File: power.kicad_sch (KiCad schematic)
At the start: 56 parts, among them J11 Conn_01x02_Pin, J13 Conn_01x02_Pin, J14 Conn_01x02_Pin, J15 Conn_01x02_Pin, J8 Conn_01x02_Pin, U10 MAX4995AAUT+T, U11 MAX4995AAUT+T, U35 MAX4995AAUT+T, U36 TPS7A5201QRGRRQ1, U4 TPSM828302ARDSR, U6 STWD100NYWY3F, U8 MP5073GG-P, U9 MAX4995AAUT+T

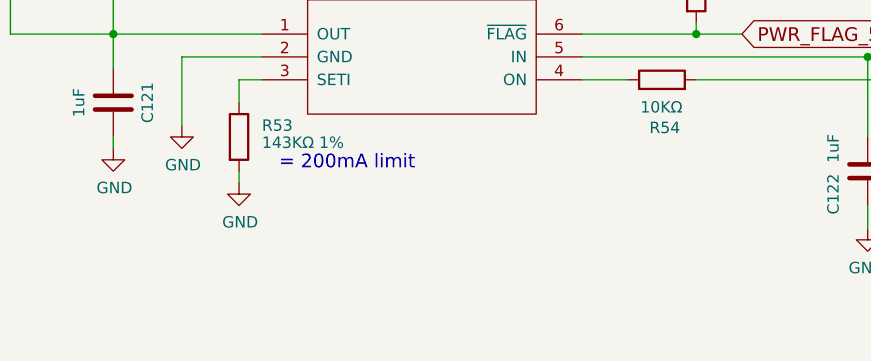
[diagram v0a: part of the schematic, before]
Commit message: Track and doc cleanups
Signed-off-by: Corey Minyard <corey@minyard.net>
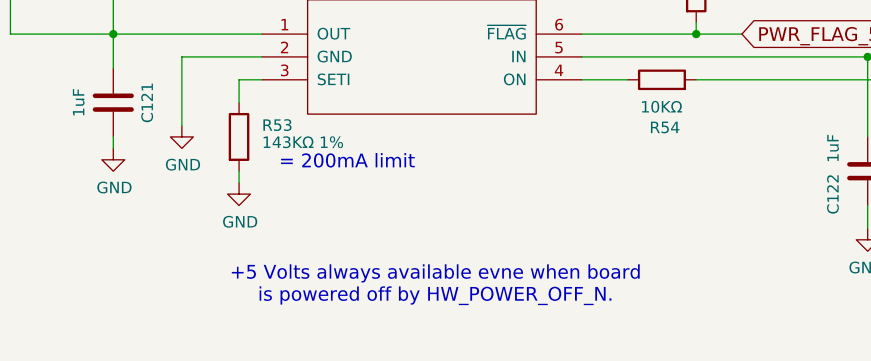
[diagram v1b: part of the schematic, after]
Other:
- note added: "+5 Volts always available evne when board is powered off by HW_POWER_OFF_N."
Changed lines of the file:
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@@
+		)
+	)
+	(text "+5 Volts always available evne when board\nis powered off by HW_POWER_OFF_N."
+		(exclude_from_sim no)
+		(at 233.934 257.81 0)
+		(effects
+			(font
+				(size 1.524 1.524)
+			)
 		)
 	)

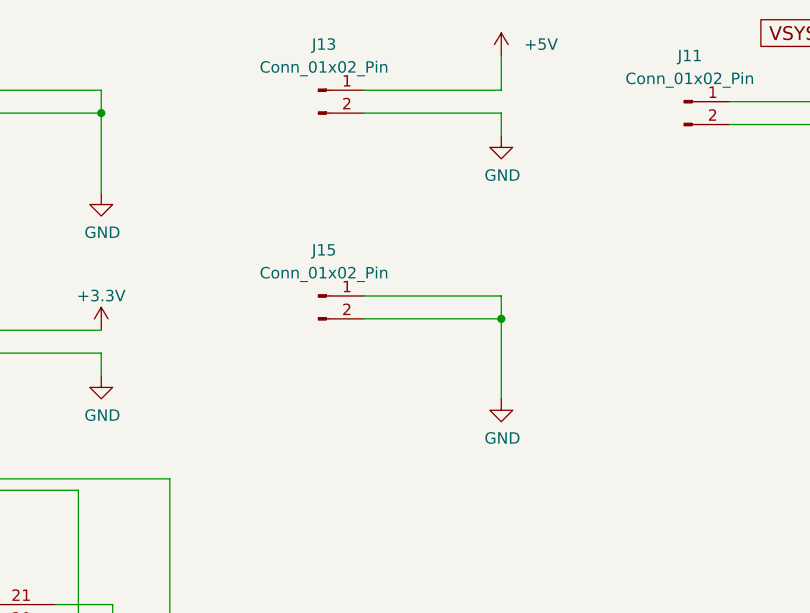
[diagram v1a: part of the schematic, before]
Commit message: Do a ton of work to switch to the CubeSat Kit Bus
Redo the connector, board shape, etc.

Signed-off-by: Corey Minyard <corey@minyard.net>
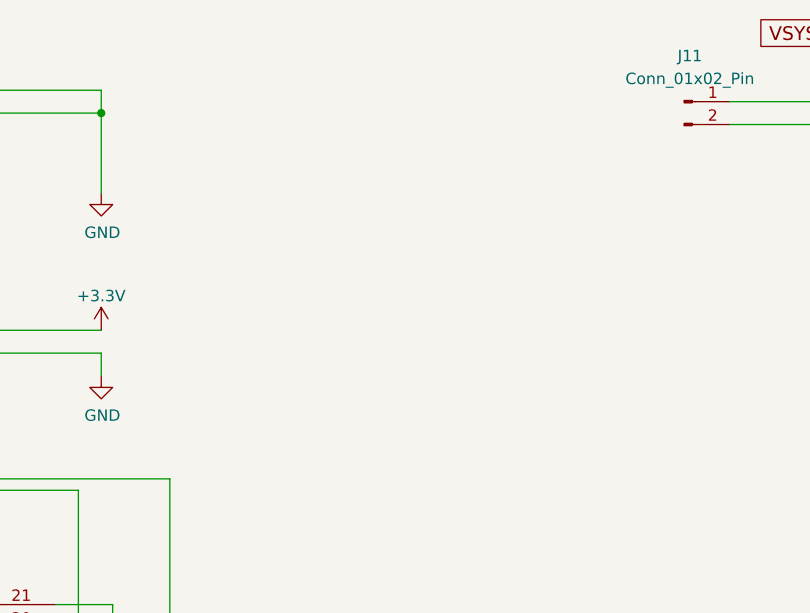
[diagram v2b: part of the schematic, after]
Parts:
- removed J13, J15: Conn_01x02_Pin, Connector_Wire:SolderWire-0.5sqmm_1x02_P4.6mm_D0.9mm_OD2.1mm, symbol Connector:Conn_01x02_Pin

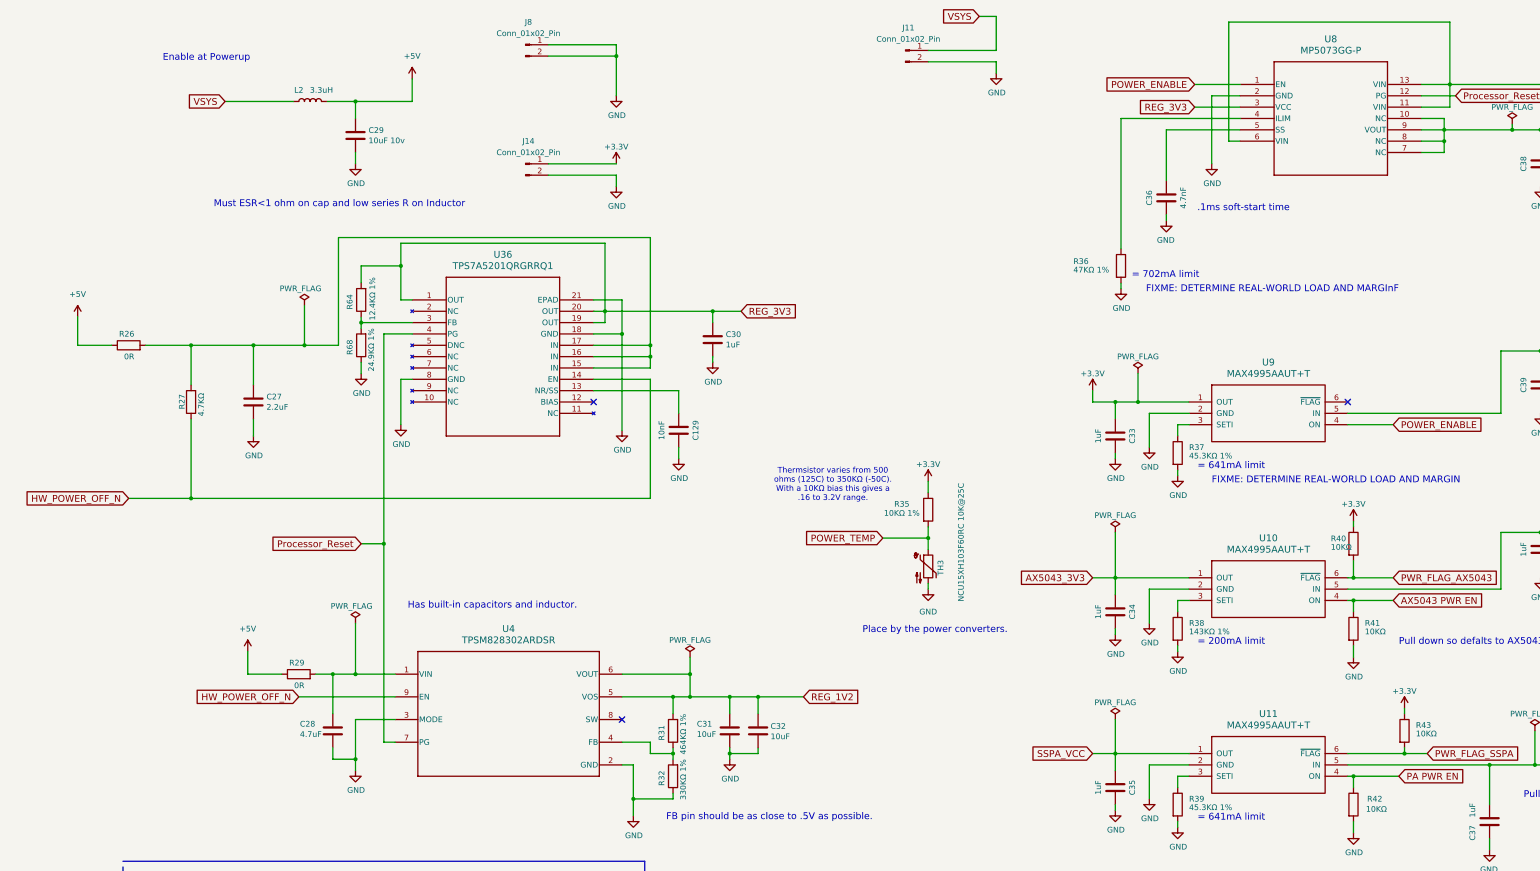
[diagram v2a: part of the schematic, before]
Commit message: More work converting to the CubeSat Kit Bus
Signed-off-by: Corey Minyard <corey@minyard.net>
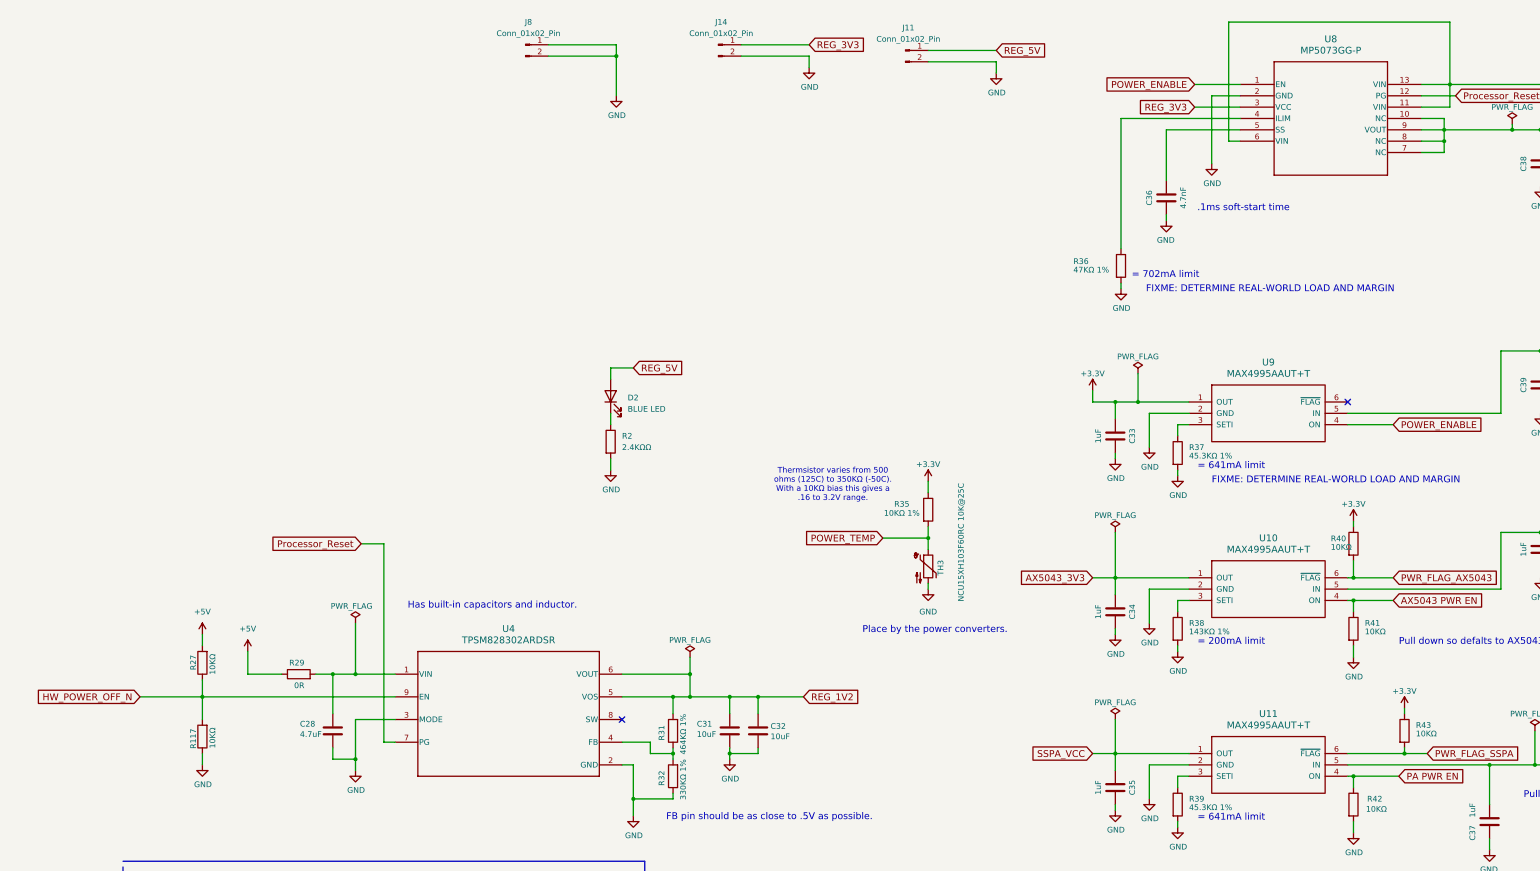
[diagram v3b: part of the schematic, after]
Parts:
- removed C129: 10nF, Capacitor_SMD:C_0402_1005Metric_Pad0.74x0.62mm_HandSolder, symbol Device:C
- removed C27: 2.2uF, Capacitor_SMD:C_0805_2012Metric_Pad1.18x1.45mm_HandSolder, symbol Device:C
- removed C29: 10uF 10v, Capacitor_SMD:C_1206_3216Metric, symbol Device:C
- removed C30: 1uF, Capacitor_SMD:C_0805_2012Metric_Pad1.18x1.45mm_HandSolder, symbol Device:C
- removed L2: 3.3uH, Inductor_SMD:L_1210_3225Metric_Pad1.42x2.65mm_HandSolder, symbol Device:L
- removed R26: 0R, Resistor_SMD:R_0603_1608Metric_Pad0.98x0.95mm_HandSolder, symbol Device:R
- removed R64: 12.4KΩ 1%, Resistor_SMD:R_0402_1005Metric_Pad0.72x0.64mm_HandSolder, symbol Device:R
- removed R68: 24.9KΩ 1%, Resistor_SMD:R_0402_1005Metric_Pad0.72x0.64mm_HandSolder, symbol Device:R
- removed U36: TPS7A5201QRGRRQ1, PacSatDev_ti:RGR20_2P05X2P05_TEX, symbol PACSAT_ICs:TPS7A5201QRGRRQ1
- added D2: BLUE LED, LED_SMD:LED_0603_1608Metric_Pad1.05x0.95mm_HandSolder, symbol Device:LED
- added R117: 10KΩ, Resistor_SMD:R_0402_1005Metric_Pad0.72x0.64mm_HandSolder, symbol Device:R
- added R2: 2.4KΩΩ, Resistor_SMD:R_0603_1608Metric_Pad0.98x0.95mm_HandSolder, symbol Device:R
- R27: value 4.7KΩ -> 10KΩ
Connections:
- net +3.3V: no longer J14.1 (Pin_1)
- net +5V: now also R27.2
- net GND: now also R117.1, R2.2
- net HW_POWER_OFF_N: now also R117.2
- net REG_3V3: now also J14.1 (Pin_1)
- net VSYS renamed REG_5V
- net REG_5V: now also D2.2 (A)
- new net: D2.1 (K), R2.1
- no-connect marks 3 -> 2
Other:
- note removed: "Enable at Powerup"
- note removed: "FIXME: DETERMINE REAL-WORLD LOAD AND MARGInF"
- note removed: "Must ESR<1 ohm on cap and low series R on Inductor"
- moved on the sheet: J14, R27

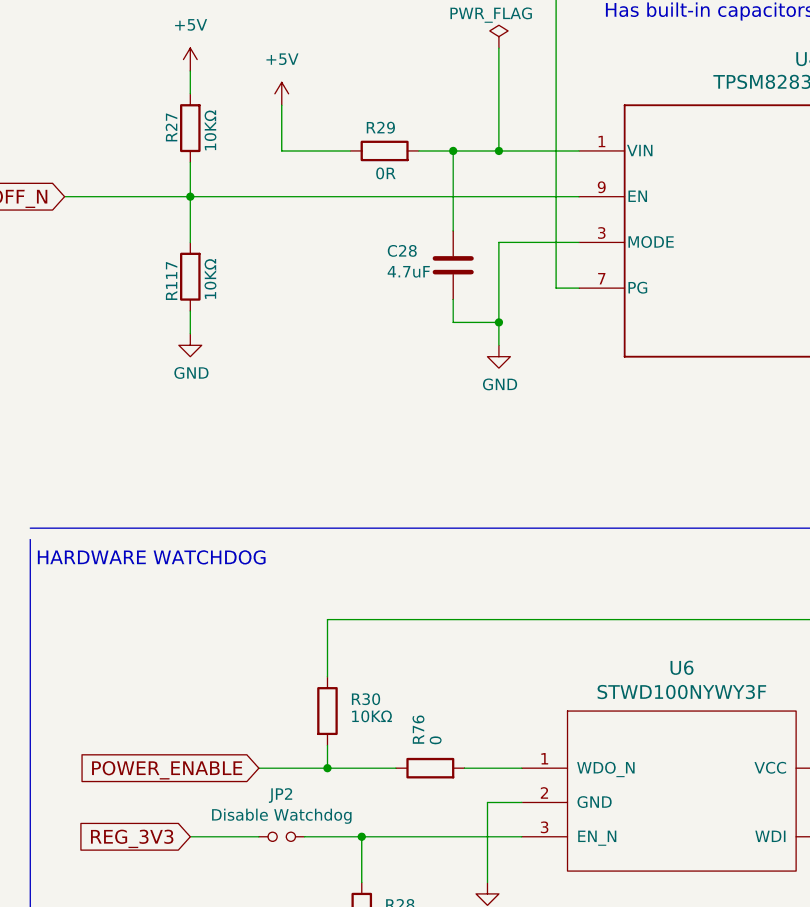
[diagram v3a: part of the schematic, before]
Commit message: Have the BOM file fixer output xls, not csv
The omega symbol gets translated properly from xls.

Signed-off-by: Corey Minyard <corey@minyard.net>
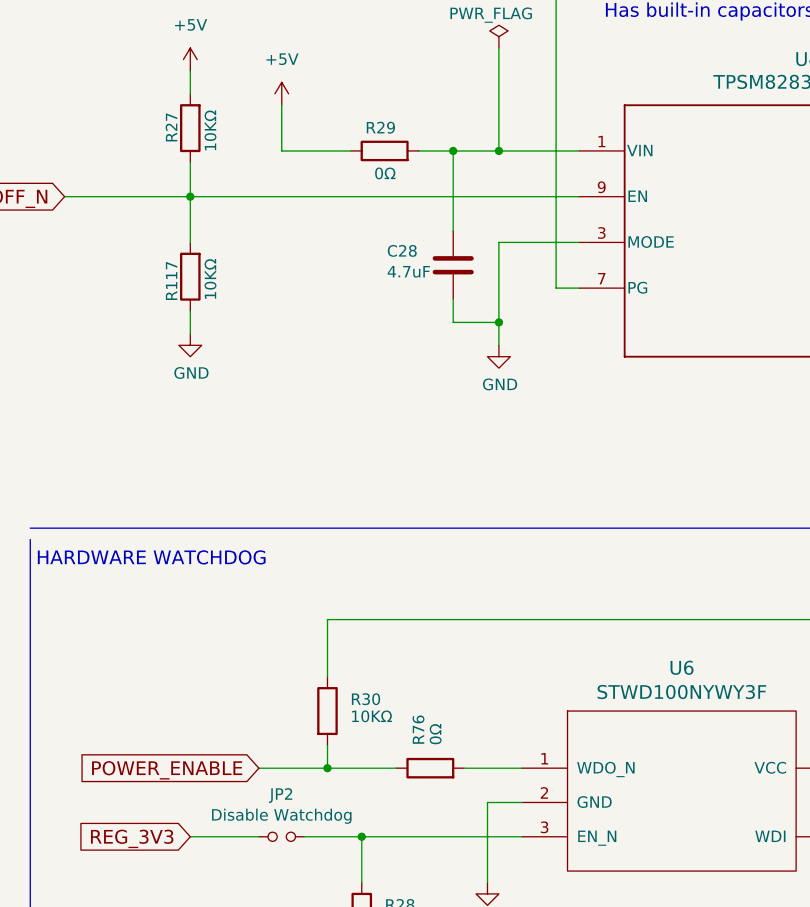
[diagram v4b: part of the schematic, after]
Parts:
- R29: value 0R -> 0Ω
- R76: value 0 -> 0Ω
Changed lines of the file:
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@@
 			)
 		)
-		(property "Value" "0R"
+		(property "Value" "0Ω"
 			(at 91.44 168.91 90)
 			(effects
@@
 			)
 		)
-		(property "Value" "0"
+		(property "Value" "0Ω"
 			(at 95.885 232.41 0)
 			(effects

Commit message: Minor fixes for BOM values
Signed-off-by: Corey Minyard <corey@minyard.net>
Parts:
- TH3: value NCU15XH103F60RC 10K@25C -> NCU15XH103F60RC 10KΩ@25C
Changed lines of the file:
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@@
 			)
 		)
-		(property "Value" "NCU15XH103F60RC 10K@25C"
+		(property "Value" "NCU15XH103F60RC 10KΩ@25C"
 			(at 238.506 150.114 90)
 			(effects

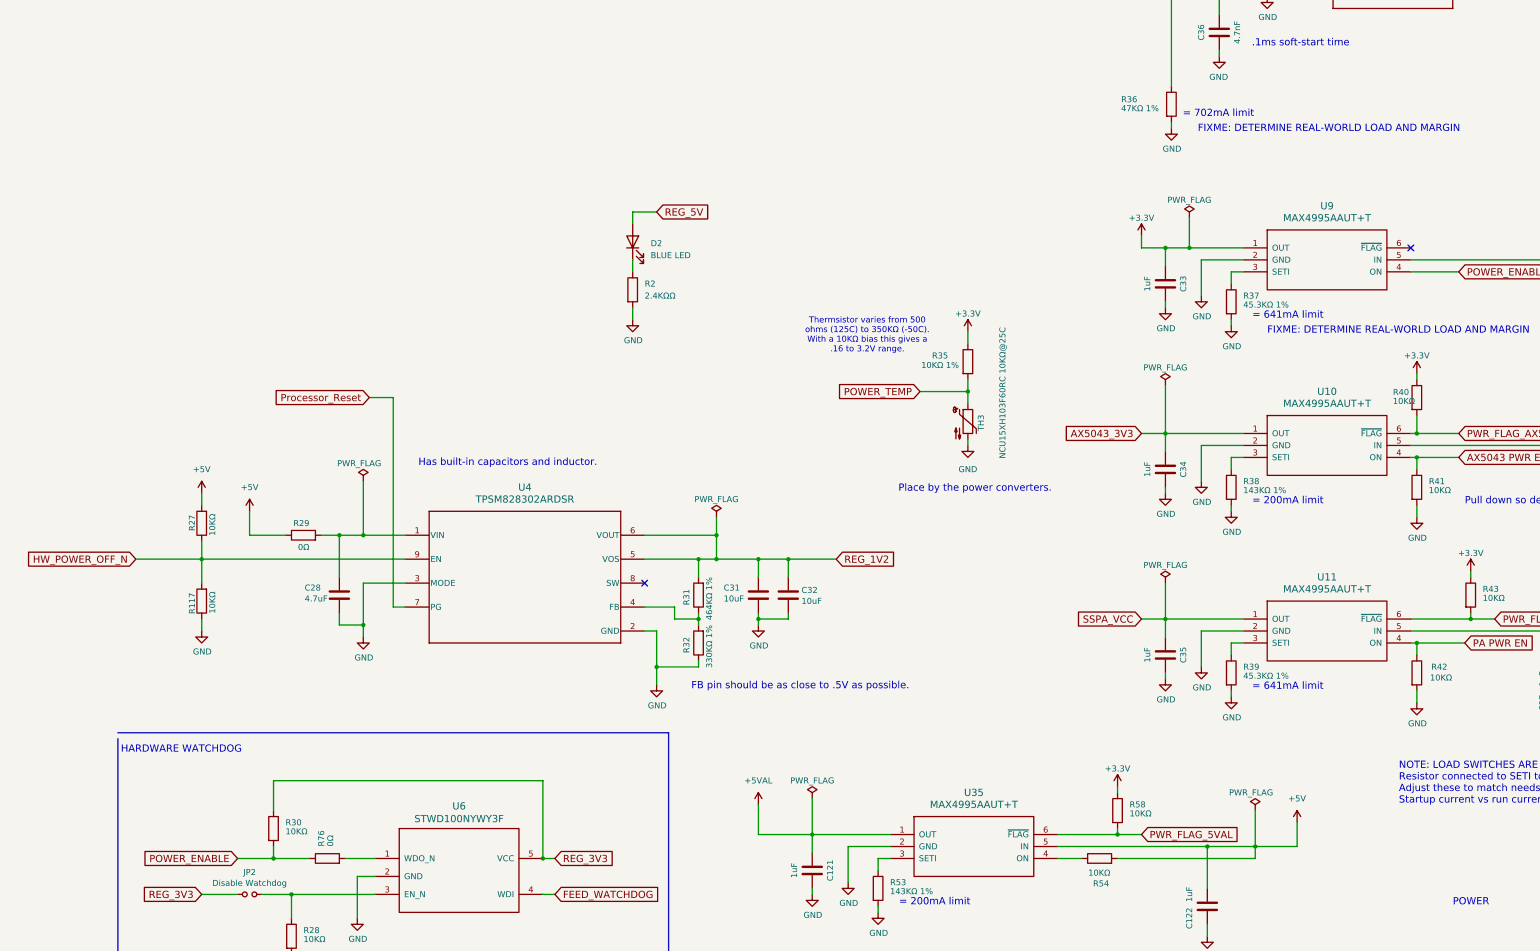
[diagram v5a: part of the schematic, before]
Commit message: Fix POWER_ENABLE to disable 3.3V
Signed-off-by: Corey Minyard <corey@minyard.net>
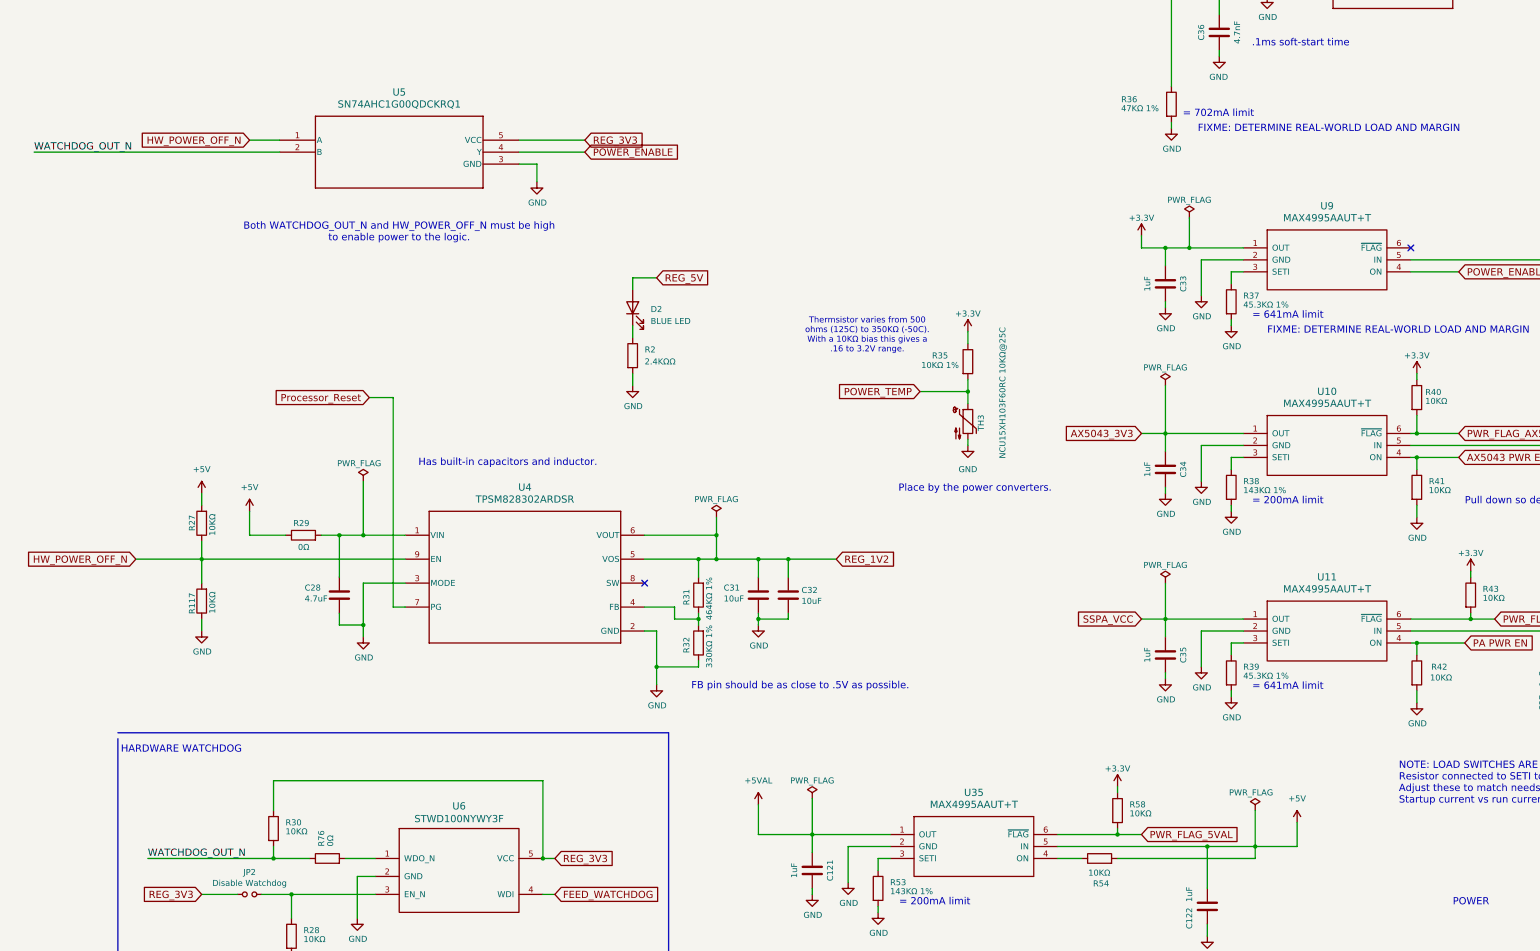
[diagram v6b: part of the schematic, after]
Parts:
- added U5: SN74AHC1G00QDCKRQ1, PacSatDev_ti:DCK5, symbol PACSAT_ICs:SN74AHC1G00QDCKRQ1
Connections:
- net GND: now also U5.3 (GND)
- net HW_POWER_OFF_N: now also U5.1 (A)
- net POWER_ENABLE: now also U5.4 (Y); no longer R30.2, R76.1
- net REG_3V3: now also U5.5 (VCC)
- new net WATCHDOG_OUT_N: R30.2, R76.1, U5.2 (B)
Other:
- note added: "Both WATCHDOG_OUT_N and HW_POWER_OFF_N must be high to enable power to the logic."
- moved on the sheet: D2, R2
